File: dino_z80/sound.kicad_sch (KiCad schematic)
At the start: 17 parts, among them J2 PJ-320D, U4 LM358

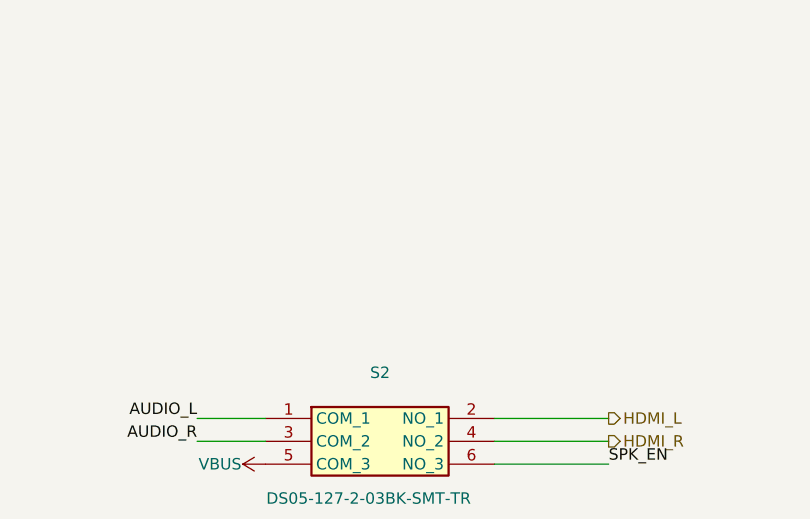
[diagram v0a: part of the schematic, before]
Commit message: feat: compact rounded solder jumpers and debug jumpers across S2
- all solder jumpers use a compact rounded footprint
  (SolderJumper-2_P1.0mm_Open_RoundedPad0.7x1.0mm: 0.7x1.0 mm pads,
  0.3 mm gap), scaled from KiCad's stock RoundedPad jumper
- JP4/JP5/JP6 (Audio L, Audio R, Speaker) bridge each S2 position, on
  the back under S2, so the DIP switch can be left unfitted
- JP3 on Dino gets short tracks to its vias, which the smaller pads no
  longer cover
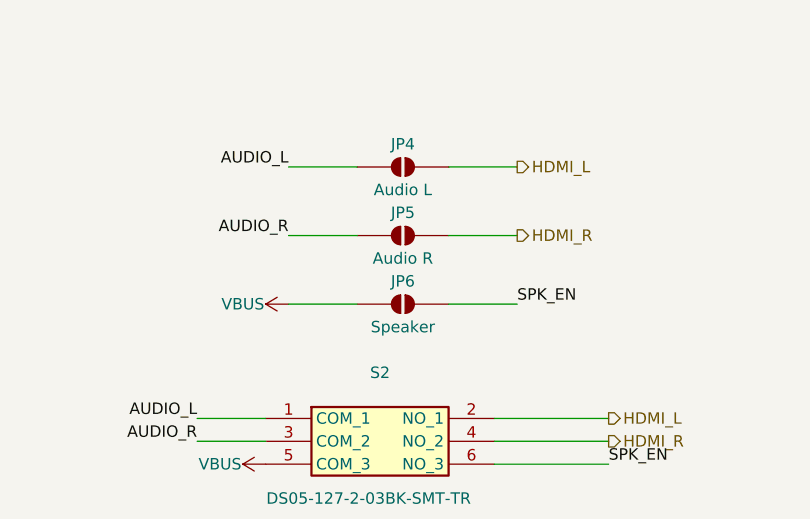
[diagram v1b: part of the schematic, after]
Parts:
- added JP4: Audio L, dino:SolderJumper-2_P1.0mm_Open_RoundedPad0.7x1.0mm, symbol dino:SolderJumper_2_Open
- added JP5: Audio R, dino:SolderJumper-2_P1.0mm_Open_RoundedPad0.7x1.0mm, symbol dino:SolderJumper_2_Open
- added JP6: Speaker, dino:SolderJumper-2_P1.0mm_Open_RoundedPad0.7x1.0mm, symbol dino:SolderJumper_2_Open
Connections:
- net AUDIO_L: now also JP4.1 (A)
- net AUDIO_R: now also JP5.1 (A)
- net HDMI_L: now also JP4.2 (B)
- net HDMI_R: now also JP5.2 (B)
- net SPK_EN: now also JP6.2 (B)
- net VBUS: now also JP6.1 (A)

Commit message: fix: board review round - protection, pull-ups, parts data
- MS9288A config I2C pull-ups (SCL/SDA) go to +3V3; the chip's pins
  are rated only to DVDD33 + 0.5 V, and the reference leaves them open
- MS9288A audio inputs: 0 Ohm series + 10 kOhm shunt (not fitted) ahead
  of the coupling caps, so the reference 1/2 divider can be fitted later
- HDMI +5 V pin: 0.2 A resettable fuse (F2, 0603) in series with D5
- SD card: 10 kOhm pull-ups on CMD, DAT0 and DAT3 (SPI mode)
- xt8086: U1 is a 74HCT04 buffering GP29 to a 5 V 8086 CLK; RESET gets a
  10 kOhm pull-up so the CPU is held in reset until the RP2350 drives it
- video ladder and headphone series resistors 400/800 -> 402/806 Ohm
- LCSC part numbers checked against JLC for 452 parts; wrong numbers on
  R57, the 4.7 uF caps and the USB-C connector fixed
- MS9288A symbol: pin 3 is NC, datasheet linked; CD4069 pin name fixed
- Dino board follows the schematic renumbering; label and via clean-up
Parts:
- C13, C14, C8: LCSC (none) -> C19702
- C5, C6: LCSC (none) -> C57112
- C7: LCSC (none) -> C14663
- J2: LCSC (none) -> C431535
- R17, R18: LCSC (none) -> C21190
- R19, R20: LCSC (none) -> C4190
- R21, R22: LCSC (none) -> C4184
- R23, R24: value 400Ω -> 402Ω; LCSC (none) -> C23049
- S2: LCSC (none) -> C3312528
- U4: LCSC (none) -> C7950
- renumbered JP4 to JP2, JP5 to JP3, JP6 to JP4

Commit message: fix: dino_z80 1.02 - pre-production review, TVS input, labels, release
- Power: SMAJ15A TVS D7 after the fuse (C908769, optional fit); Q1 gate
  divider R47/R48 100K/43K (Vgs within +-12 V at the TVS clamp); MP1584 UVLO
  R50/R51 300K/100K (start ~6.0 V); C54 680u 25V (C46550437); notes fixed
- Every capacitor value carries its voltage (from the LCSC part)
- Test points on all rails, on the back
- ERC: connector/hub pin types, PWR_FLAGs; 49 stale exclusions removed.
  ERC 0 errors, 0 warnings
- RP2350 exposed-pad vias tagged heatsink (no type mismatch)
- Fields: LCSC numbers removed from solder jumpers, S1/U1/U2/Y2/L1 part
  data and datasheet links corrected
- Layout: vias moved out of signal/power pads where a 45-degree escape
  exists, corners fixed, reference labels 0.7 mm bold re-placed
- Release 1.02: gerbers, schematics, assembly PDF, iBOM
  (DRC 0 violations, 0 unconnected, 0 parity)
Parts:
- C13, C14, C8: value 10µF -> 10u 10V
- C5, C6: value 10nF -> 10n 50V
- C7: value 100nF -> 100n 50V
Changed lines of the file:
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@@
 			)
 		)
-		(property "Value" "10nF"
+		(property "Value" "10n 50V"
 			(at 62.23 88.9 90)
 			(show_name no)
@@
 			)
 		)
-		(property "Value" "10µF"
+		(property "Value" "10u 10V"
 			(at 143.51 48.26 90)
 			(show_name no)
@@
 			)
 		)
-		(property "Value" "100nF"
+		(property "Value" "100n 50V"
 			(at 133.35 48.26 90)
 			(show_name no)
@@
 			)
 		)
-		(property "Value" "10µF"
+		(property "Value" "10u 10V"
 			(at 237.49 110.49 270)
 			(show_name no)
@@
 			)
 		)
-		(property "Value" "10nF"
+		(property "Value" "10n 50V"
 			(at 62.23 127 90)
 			(show_name no)
@@
 			)
 		)
-		(property "Value" "10µF"
+		(property "Value" "10u 10V"
 			(at 237.49 119.38 270)
 			(show_name no)
